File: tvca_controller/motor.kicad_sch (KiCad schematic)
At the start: 3 parts, among them J3 Encoder Connection - ATM103-V, J5 Motor Connector, U3 BD6222HFP

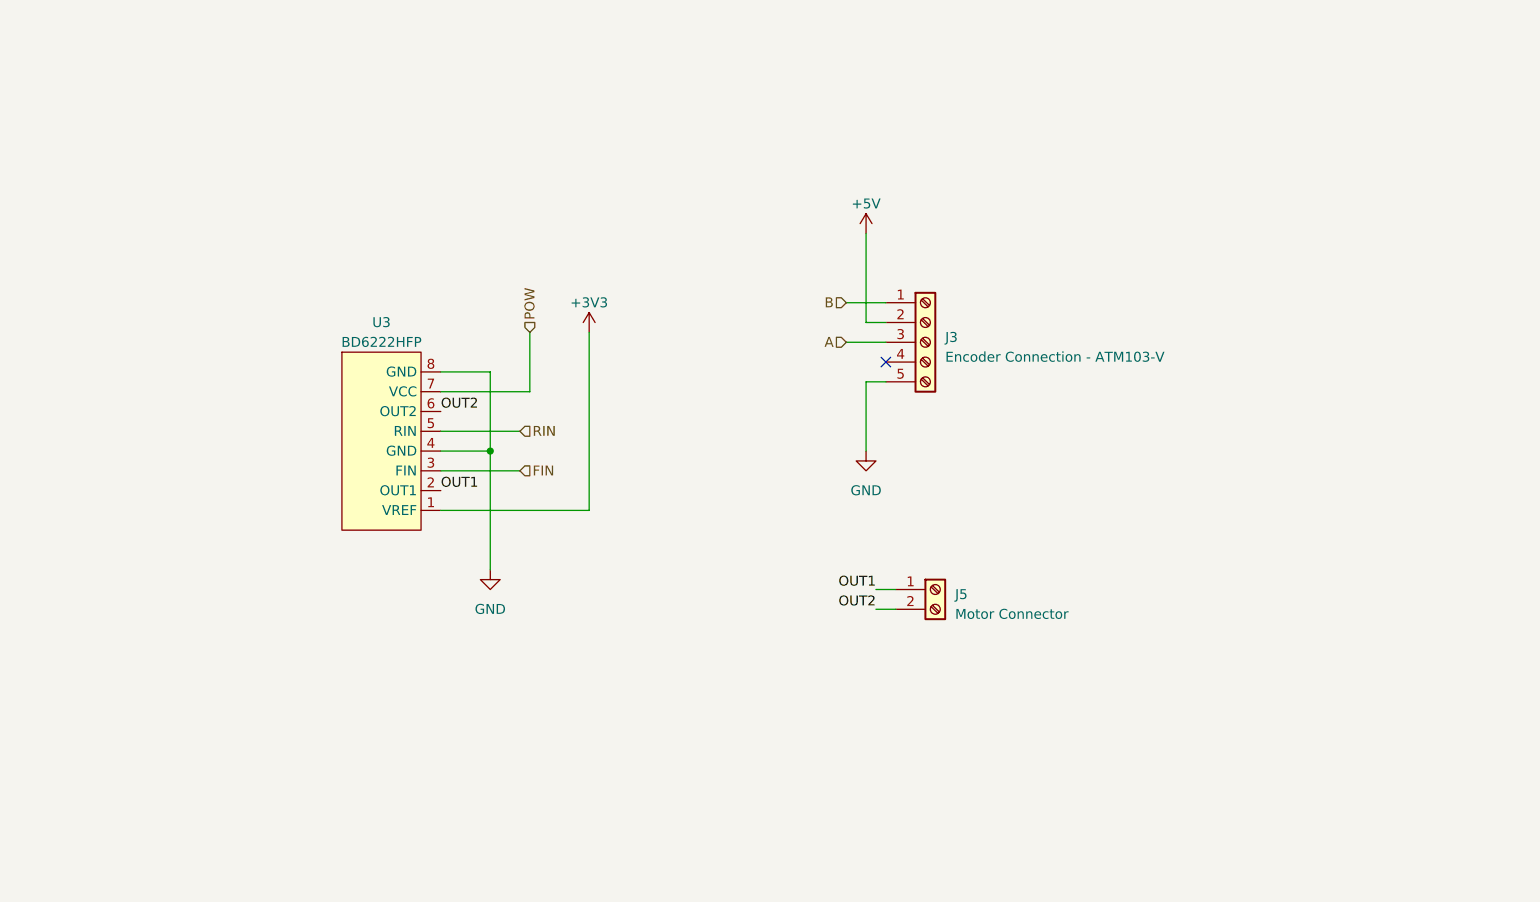
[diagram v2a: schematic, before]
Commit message: add current and voltage sensing. Address minor fixes suggested by Jack. Ready for final review
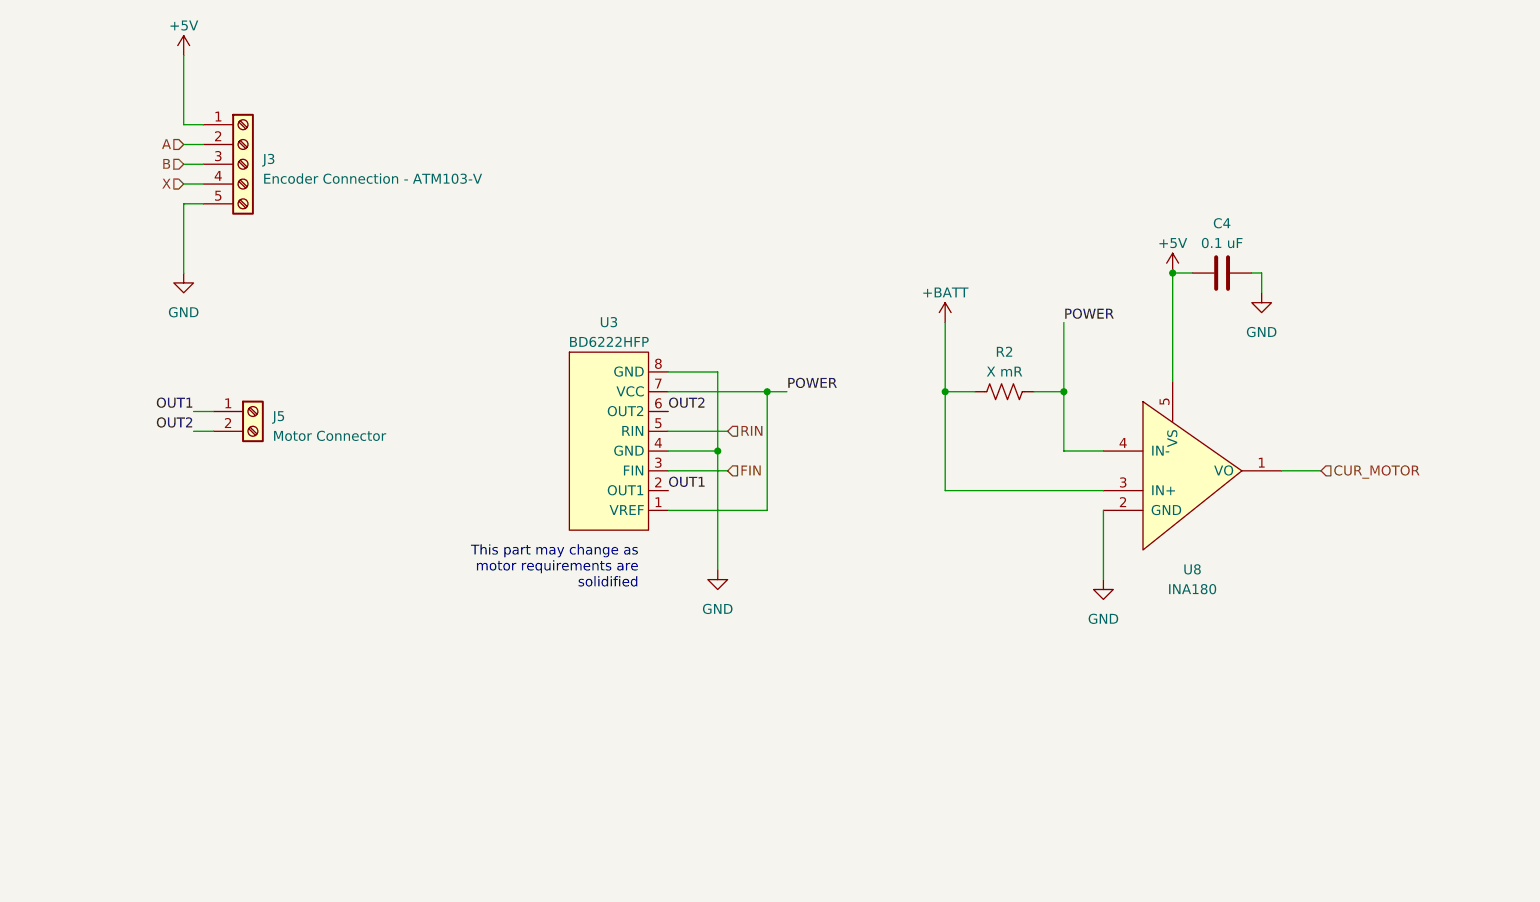
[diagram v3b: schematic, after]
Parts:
- added C4: 0.1 uF, symbol Device:C
- added R2: X mR, symbol Device:R_US
- added U8: INA180, symbol canhw:INA180
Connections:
- net POW is gone; now on net POWER: U3.7 (VCC)
- net +5V: now also J3.1 (Pin_1), C4.1, U8.5 (VS); no longer J3.2 (Pin_2)
- net A: now also J3.2 (Pin_2); no longer J3.3 (Pin_3)
- net B: now also J3.3 (Pin_3); no longer J3.1 (Pin_1)
- net GND: now also C4.2, U8.2 (GND)
- net X: now reaches J3.4 (Pin_4)
- net +3V3 renamed POWER
- net POWER: now also R2.1, U8.4 (IN-)
- new net +BATT: R2.2, U8.3 (IN+)
- new net CUR_MOTOR: U8.1 (VO)
- no-connect marks 1 -> 0
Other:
- note added: "This part may change as motor requirements are solidified"
- moved on the sheet: J3, J5, U3

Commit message: Add foot prints, numerous other small changes
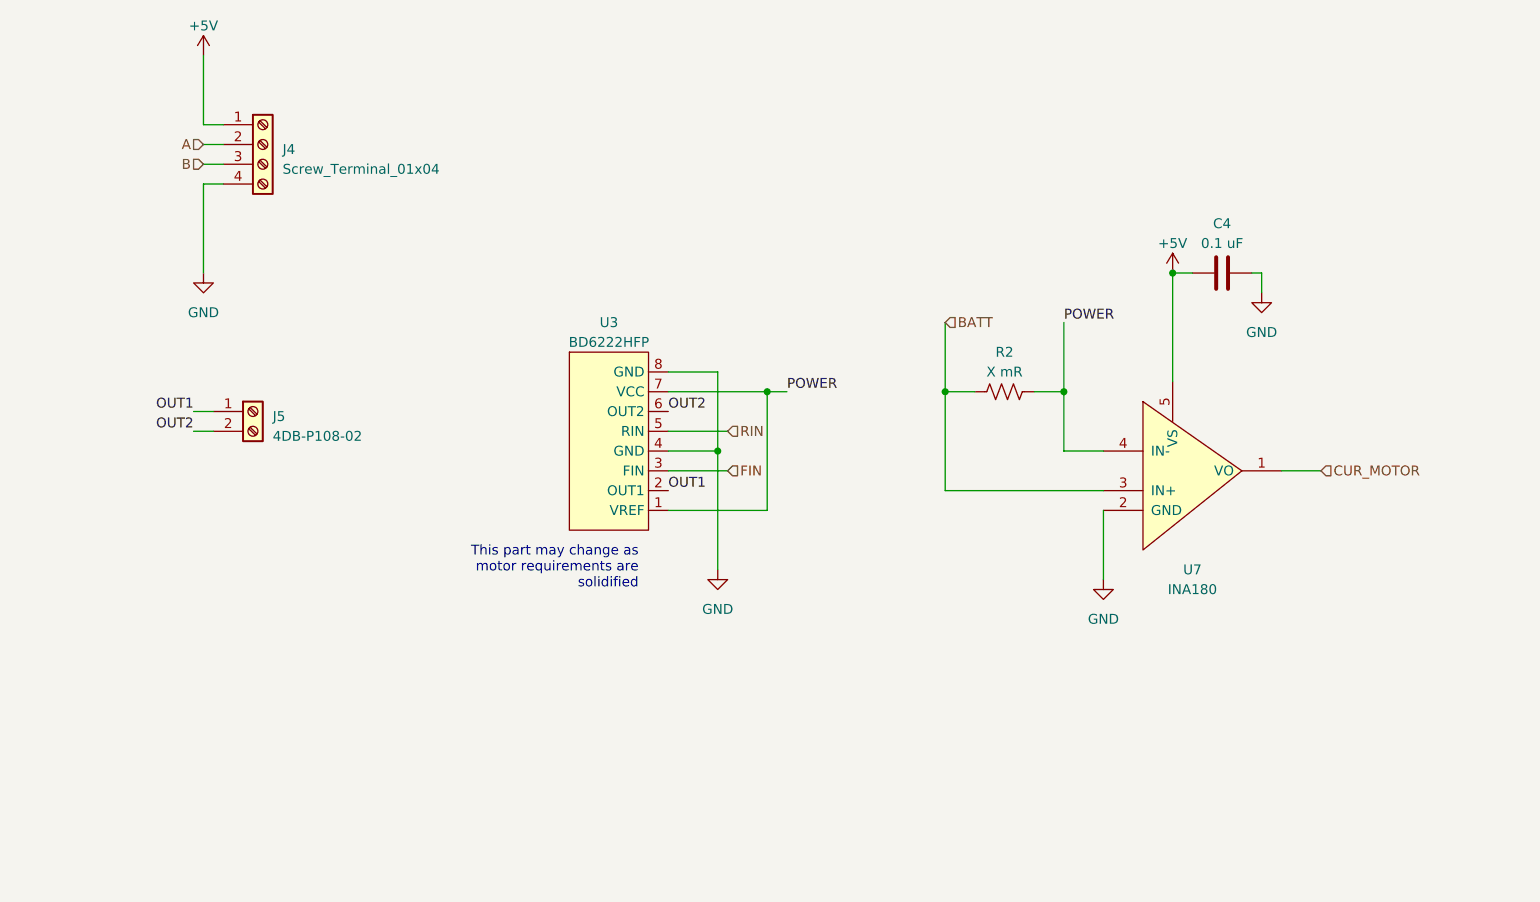
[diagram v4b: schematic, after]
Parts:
- removed J3: Encoder Connection - ATM103-V, symbol Connector:Screw_Terminal_01x05
- added J4: Screw_Terminal_01x04, TerminalBlock_Phoenix:TerminalBlock_Phoenix_PT-1,5-4-5.0-H_1x04_P5.00mm_Horizontal, symbol Connector:Screw_Terminal_01x04
- C4: footprint (none) -> Capacitor_SMD:C_0805_2012Metric_Pad1.18x1.45mm_HandSolder
- J5: value Motor Connector -> 4DB-P108-02; footprint (none) -> canhw_footprints:TE_2-1437667-4
- R2: footprint (none) -> Resistor_SMD:R_0805_2012Metric_Pad1.20x1.40mm_HandSolder
- U3: footprint (none) -> Package_TO_SOT_SMD:Rohm_HRP7
- U7: renamed from U8; footprint (none) -> Package_TO_SOT_SMD:SOT-23-5_HandSoldering
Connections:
- net +5V: now also J4.1 (Pin_1)
- net A: now also J4.2 (Pin_2)
- net B: now also J4.3 (Pin_3)
- net GND: now also J4.4 (Pin_4)
- net +BATT renamed BATT

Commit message: shize shunt resistor
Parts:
- R2: value X mR -> 2 mR
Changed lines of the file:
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@@
       (effects (font (size 1.27 1.27)))
     )
-    (property "Value" "X mR" (at 180.34 81.28 90)
+    (property "Value" "2 mR" (at 180.34 81.28 90)
       (effects (font (size 1.27 1.27)))
     )

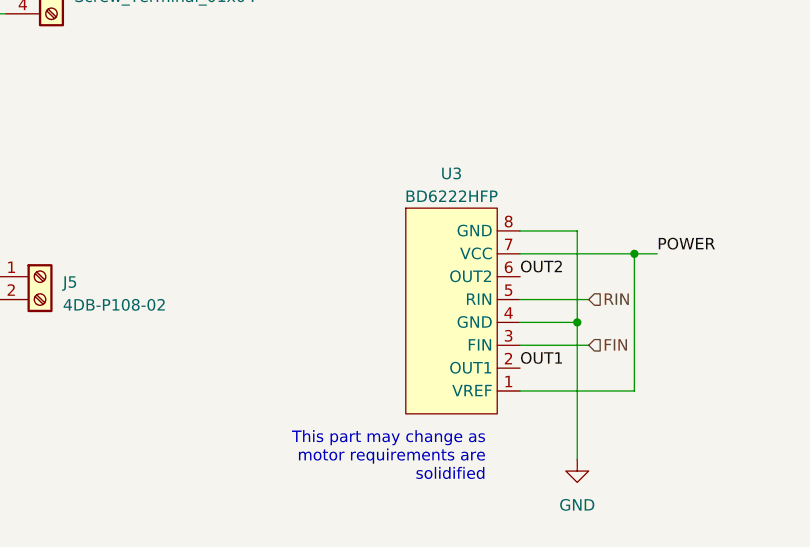
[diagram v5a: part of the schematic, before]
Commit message: Finish up schematic for jack to review, start PCB layout
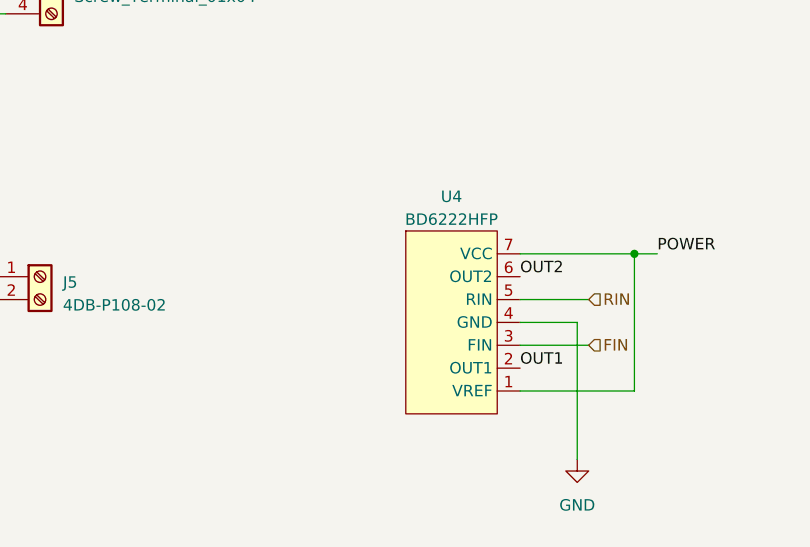
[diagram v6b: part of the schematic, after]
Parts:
- removed U3: BD6222HFP, Package_TO_SOT_SMD:Rohm_HRP7, symbol TVCA_symbols:BD6222HFP
- added U4: BD6222HFP, Package_TO_SOT_SMD:Rohm_HRP7, symbol TVCA_symbols:BD6222HFP
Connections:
- net FIN: now also U4.3 (FIN)
- net GND: now also U4.4 (GND)
- net OUT1: now also U4.2 (OUT1)
- net OUT2: now also U4.6 (OUT2)
- net POWER: now also U4.1 (VREF), U4.7 (VCC)
- net RIN: now also U4.5 (RIN)
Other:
- note removed: "This part may change as motor requirements are solidified"

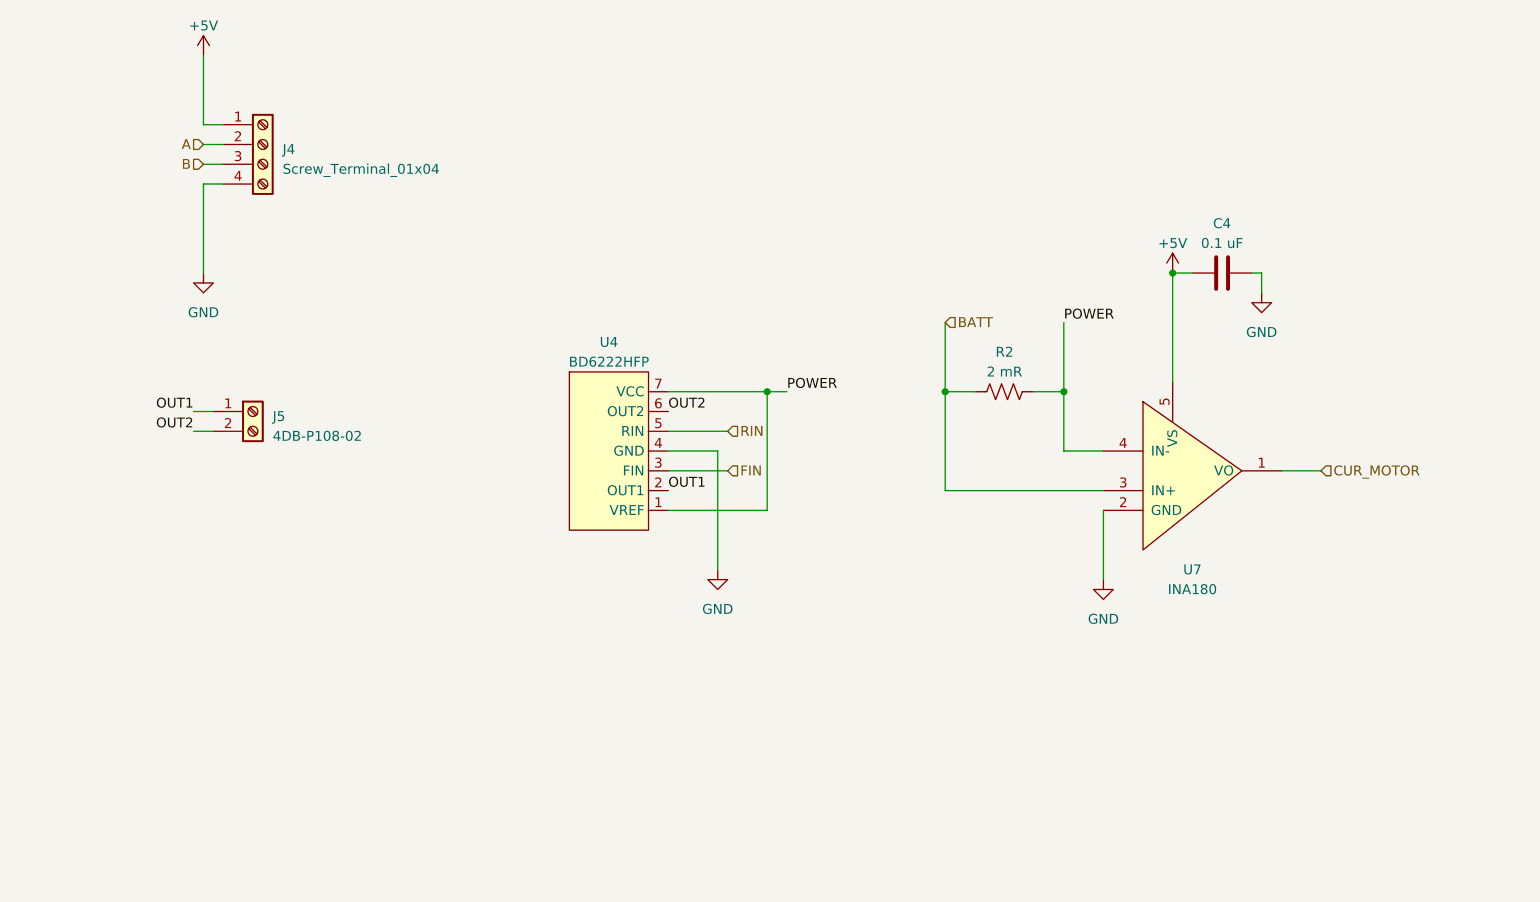
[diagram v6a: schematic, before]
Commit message: Replace motor controller IC
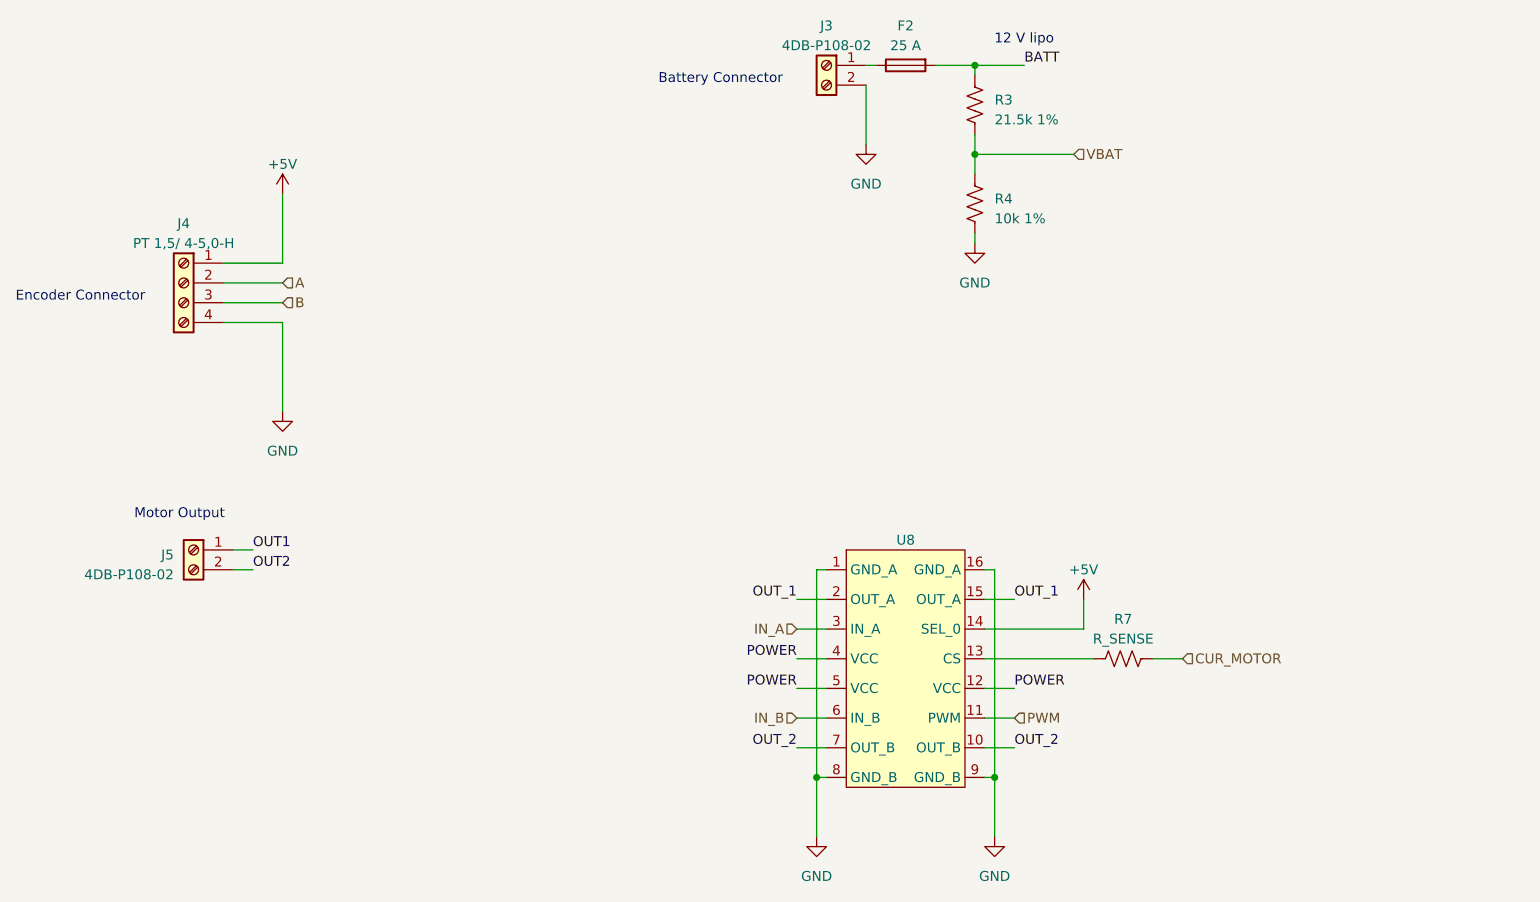
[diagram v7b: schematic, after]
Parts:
- removed C4: 0.1 uF, Capacitor_SMD:C_0805_2012Metric_Pad1.18x1.45mm_HandSolder, symbol Device:C
- removed R2: 2 mR, Resistor_SMD:R_0805_2012Metric_Pad1.20x1.40mm_HandSolder, symbol Device:R_US
- removed U4: BD6222HFP, Package_TO_SOT_SMD:Rohm_HRP7, symbol TVCA_symbols:BD6222HFP
- removed U7: INA180, Package_TO_SOT_SMD:SOT-23-5_HandSoldering, symbol canhw:INA180
- added F2: 25 A, Fuse:Fuseholder_Cylinder-6.3x32mm_Schurter_0031-8002_Horizontal_Open, symbol Device:Fuse
- added J3: 4DB-P108-02, canhw_footprints:TE_2-1437667-4, symbol Connector:Screw_Terminal_01x02
- added R3: 21.5k 1%, Resistor_SMD:R_0805_2012Metric_Pad1.20x1.40mm_HandSolder, symbol Device:R_US
- added R4: 10k 1%, Resistor_SMD:R_0805_2012Metric_Pad1.20x1.40mm_HandSolder, symbol Device:R_US
- added R7: R_SENSE, Resistor_SMD:R_0805_2012Metric_Pad1.20x1.40mm_HandSolder, symbol Device:R_US
- added U8: ~, Package_SO:SO-16_3.9x9.9mm_P1.27mm, symbol TVCA_symbols:VNH7070AS
- J4: value Screw_Terminal_01x04 -> PT 1,5/ 4-5,0-H
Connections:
- net +5V: now also U8.14 (SEL_0)
- net BATT: now also F2.2, R3.1
- net CUR_MOTOR: now also R7.1
- net GND: now also J3.2 (Pin_2), R4.2, U8.1 (GND_A), U8.16 (GND_A), U8.8 (GND_B), U8.9 (GND_B)
- net POWER: now also U8.12 (VCC), U8.4 (VCC), U8.5 (VCC)
- new net: F2.1, J3.1 (Pin_1)
- new net: R7.2, U8.13 (CS)
- new net IN_A: U8.3 (IN_A)
- new net IN_B: U8.6 (IN_B)
- new net OUT_1: U8.15 (OUT_A), U8.2 (OUT_A)
- new net OUT_2: U8.10 (OUT_B), U8.7 (OUT_B)
- new net PWM: U8.11 (PWM)
- new net VBAT: R3.2, R4.1
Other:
- note added: "12 V lipo"
- note added: "Battery Connector"
- note added: "Encoder Connector"
- note added: "Motor Output"
- moved on the sheet: J4, J5
